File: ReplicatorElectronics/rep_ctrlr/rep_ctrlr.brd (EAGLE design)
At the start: 100 x 80 mm, 108 parts, among them IC1 MICROCHIP_PIC32MX7X5F256L-PF, IC2 MICROCHIP_MCP6001-LT, IC3 MICROCHIP_MCP6001-LT, IC4 MICROCHIP_MCP6001-LT, IC5 MICROCHIP_MCP6001-LT, J1 ATX24RH, J10 SBH11-PBPC-D07-ST-BK, J11 SBH11-PBPC-D07-ST-BK, J12 SBH11-PBPC-D07-ST-BK, J13 SBH11-PBPC-D07-ST-BK, J14 SBH11-PBPC-D07-ST-BK, J15 SBH11-PBPC-D07-ST-BK, J16 SBH11-PBPC-D07-ST-BK, J17 SBH11-PBPC-D07-ST-BK, J18 SI-50170-F, J19 70553-0106, J3 FPS009-3003, J4 RJ11-2L-B, J6 SBH11-PBPC-D05-ST-BK, J7 SBH11-PBPC-D05-ST-BK, J8 SBH11-PBPC-D05-ST-BK, J9 SBH11-PBPC-D05-ST-BK, U18 LDS3985XX33, X1 CMR3XXT, X2 CMR3XXT

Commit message: 5/5/12: Routed good portion of the PHY. Work in progress.
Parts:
- moved R42 155.6 mm to (78.9, 62.6)
- moved R35 154.5 mm to (82.0, 48.5), turned to 90 degrees
- moved R45 153.2 mm to (64.8, 58.5)
- moved R41 150.0 mm to (79.0, 64.9), turned to 180 degrees
- moved R34 147.2 mm to (79.0, 48.5), turned to 90 degrees
- moved R33 140.3 mm to (76.0, 48.0), turned to 90 degrees
- moved C27 137.5 mm to (73.8, 61.2), turned to 90 degrees
- moved R31 133.4 mm to (80.5, 52.0), turned to 90 degrees
- moved R32 133.2 mm to (73.0, 48.2), turned to 90 degrees
- moved C29 131.9 mm to (67.6, 53.5)
- moved C28 130.6 mm to (76.0, 61.2), turned to 90 degrees
- moved C25 129.0 mm to (68.5, 47.5), turned to 180 degrees
- moved C26 128.8 mm to (69.8, 60.0), turned to 180 degrees
- moved R30 126.4 mm to (77.5, 52.0), turned to 90 degrees
- moved C24 122.2 mm to (68.5, 50.2), turned to 180 degrees
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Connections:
- removed net N$22: C29.1
- new net ETXEN: IC1.67, R27.1
- net DGND: now also C29.1
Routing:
- net ECRSDV: track 0.00 -> 52.5 mm, vias 0 -> 4
- net NRST: track 0.00 -> 35.3 mm, vias 0 -> 2
- net N$38: track 0.00 -> 35.2 mm, vias 0 -> 2
- net ERXD0: track 0.00 -> 33.7 mm, vias 0 -> 2
- net EREFCLK: track 0.00 -> 29.5 mm, vias 0 -> 2
- net ETH_3_3V: track 0.00 -> 29.3 mm, vias 0 -> 2
- net N$39: track 0.00 -> 29.0 mm, vias 0 -> 2
- net ERXD1: track 0.00 -> 27.4 mm, vias 0 -> 2
- net LED1: track 0.00 -> 26.1 mm, vias 0 -> 1
- net ERXERR: track 0.00 -> 25.0 mm
- net N$30: track 0.00 -> 16.7 mm, vias 0 -> 2
- net N$33: track 0.00 -> 14.1 mm, vias 0 -> 2
- net N$32: track 0.00 -> 9.79 mm, vias 0 -> 2
- net EMDIO: track 0.00 -> 9.57 mm, vias 0 -> 2
- net N$31: track 0.00 -> 9.49 mm, vias 0 -> 2
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- added copper zone on layer 1, net DGND
- added copper zone on layer 16, net DGND
- removed copper zone on layer 16, net GND

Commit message: 5/8/12: First complete PHY layout attempt. Other parts of board still require routing.
~ 2 hrs.
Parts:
- removed Q1: (no value), semicon-smd-ipc:SOT23
- removed R10, R11, R12, R9: 22, resistor:R0603
- removed U$1: PETERATMEGA644_LCD37, microtouch:PETERATMEGA644_LCD371MM
- moved R26 204.9 mm to (86.5, 44.8), turned to 90 degrees
- moved R25 202.6 mm to (88.0, 41.2), turned to 90 degrees
- moved R38 177.4 mm to (71.2, 60.2), turned to 90 degrees
- moved R39 175.7 mm to (64.5, 60.2), turned to 90 degrees
- moved R37 170.2 mm to (69.0, 60.2), turned to 90 degrees
- moved R44 170.2 mm to (84.4, 49.4), turned to 180 degrees
- moved C23 167.0 mm to (82.5, 67.8), turned to 90 degrees
- moved C22 157.3 mm to (77.2, 67.9), turned to 90 degrees
- moved R43 133.5 mm to (55.7, 60.8), turned to 180 degrees
- moved R36 46.0 mm to (63.8, 54.5), turned to 90 degrees
- moved R27 39.2 mm to (85.0, 41.2), turned to 90 degrees
- moved R40 24.5 mm to (66.8, 60.2)
- moved C28 19.4 mm to (59.5, 51.0), turned to 0 degrees
- moved C24 16.5 mm to (53.2, 56.5)
- moved C25 16.4 mm to (53.0, 52.8)
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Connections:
- removed net LCD_LED: Q1.1
- removed net N$1: R9.2, U$1.17
- removed net N$10: Q1.3, R10.1, R11.1, R12.1, R9.1
- removed net N$3: R10.2, U$1.18
- removed net N$4: R11.2, U$1.19
- removed net N$6: R12.2, U$1.20
- new net N$54: IC1.79
- new net N$55: IC1.80
- net A0: no longer U$1.8
- net DB0: no longer U$1.1
- net DB1: no longer U$1.2
- net DB10: no longer U$1.23
- net DB11: no longer U$1.24
- net DB14: no longer IC1.79, U$1.25
- net DB15: no longer IC1.80, U$1.26
- net DB16: no longer U$1.27, U$1.29
- net DB17: no longer U$1.28, U$1.30
- net DB2: no longer U$1.3
- net DB3: no longer U$1.4
- net DB4: no longer U$1.22
- net DB5: no longer U$1.35
- net DB6: no longer U$1.36
- net DB7: no longer U$1.37
- net DGND: now also J10.10, J10.12, J11.10, J11.12, J12.10, J12.12, J13.10, J13.12, J14.10, J14.12, J15.10, J15.12, J16.10, J16.12, J17.10, J17.12; no longer Q1.2, U$1.11, U$1.21, U$1.34, U$1.5
- net ENC_3_3V: now also J10.14, J11.14, J12.14, J13.14, J14.14, J15.14, J16.14, J17.14
- net GND: now also J10.2, J10.4, J10.6, J11.2, J11.4, J11.6, J12.2, J12.4, J12.6, J13.2, J13.4, J13.6, J14.2, J14.4, J14.6, J15.2, J15.4, J15.6, J16.2, J16.4, J16.6, J17.2, J17.4, J17.6
- net LCD_CS: no longer U$1.7
- net LCD_RD: no longer U$1.10
- net LCD_RST: no longer U$1.31
- net LCD_WR: no longer U$1.9
- net SERVO0: now also J10.8
- net SERVO1: now also J11.8
- net SERVO2: now also J12.8
- net SERVO3: now also J13.8
- net SERVO4: now also J14.8
- net SERVO5: now also J15.8
- net SERVO6: now also J16.8
- net SERVO7: now also J17.8
- net VCC: no longer U$1.16, U$1.32, U$1.33, U$1.6
- net X+: no longer U$1.12
- net X-: no longer U$1.14
- net Y+: no longer U$1.13
- net Y-: no longer U$1.15
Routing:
- net ENC_3_3V: track 9.47 -> 112.5 mm, vias 1 -> 5
- net ENC_SCK: track 0.00 -> 57.5 mm
- net ENC_MOSI: track 0.00 -> 57.1 mm
- net ENC_MISO: track 0.00 -> 56.4 mm
- net N$36: track 0.00 -> 51.0 mm, vias 0 -> 4
- net LED2: track 7.83 -> 57.0 mm, vias 0 -> 3
- net N$37: track 0.00 -> 40.7 mm, vias 0 -> 2
- net ETXD0: track 0.00 -> 39.8 mm, vias 0 -> 2
- net N$34: track 0.00 -> 36.9 mm, vias 0 -> 2
- net ETXD1: track 0.00 -> 35.9 mm, vias 0 -> 2
- net N$35: track 0.00 -> 32.6 mm, vias 0 -> 1
- net ETH_3_3V: track 29.3 -> 53.0 mm, vias 2 -> 5
- net N$23: track 0.00 -> 23.0 mm, vias 0 -> 2
- net ETXEN: track 0.00 -> 19.4 mm, vias 0 -> 2
- net N$25: track 0.00 -> 17.4 mm, vias 0 -> 2
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- added copper zone on layer 16, net 5V_SERVO
- added copper zone on layer 1, net ENC_3_3V
- added copper zone on layer 1, net ETH_3_3V

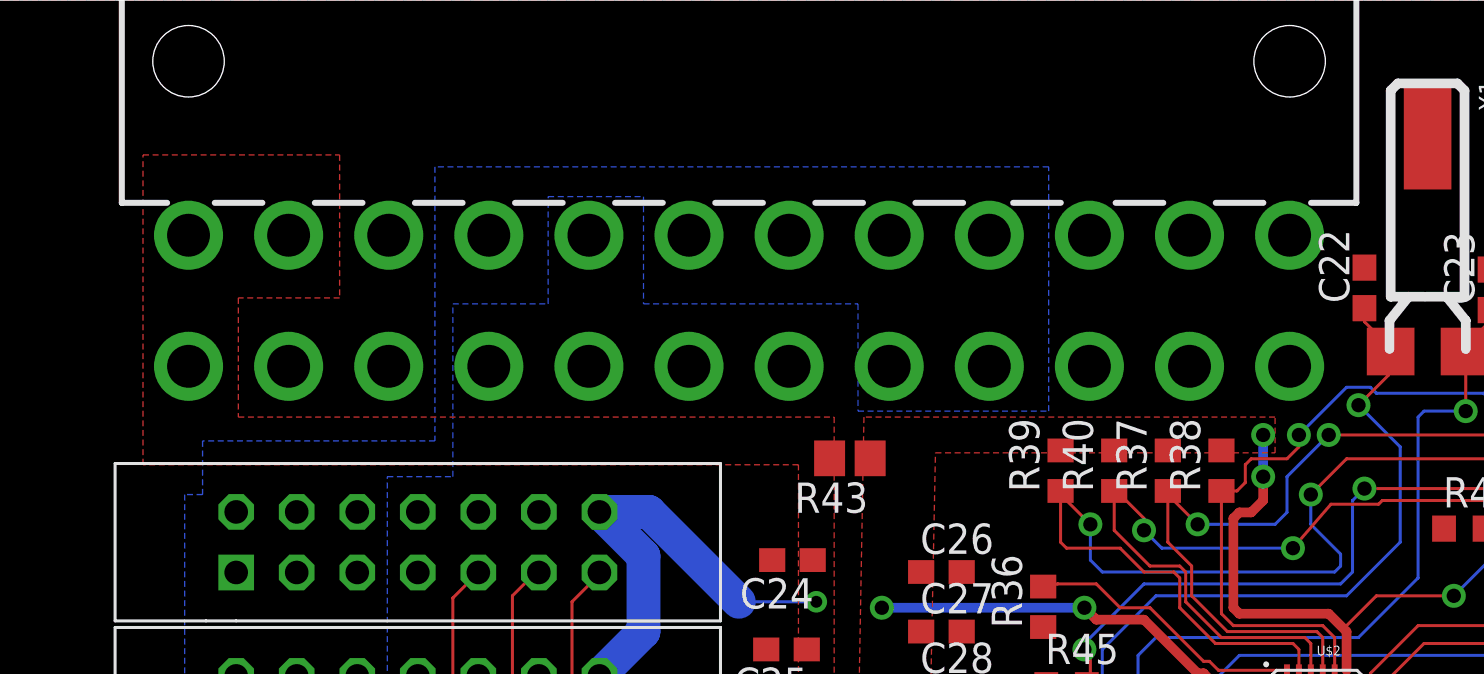
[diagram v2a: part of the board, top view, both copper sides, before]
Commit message: 5/8/12: Tied last 3.3V pin on ATX conn to ENC_3_3V
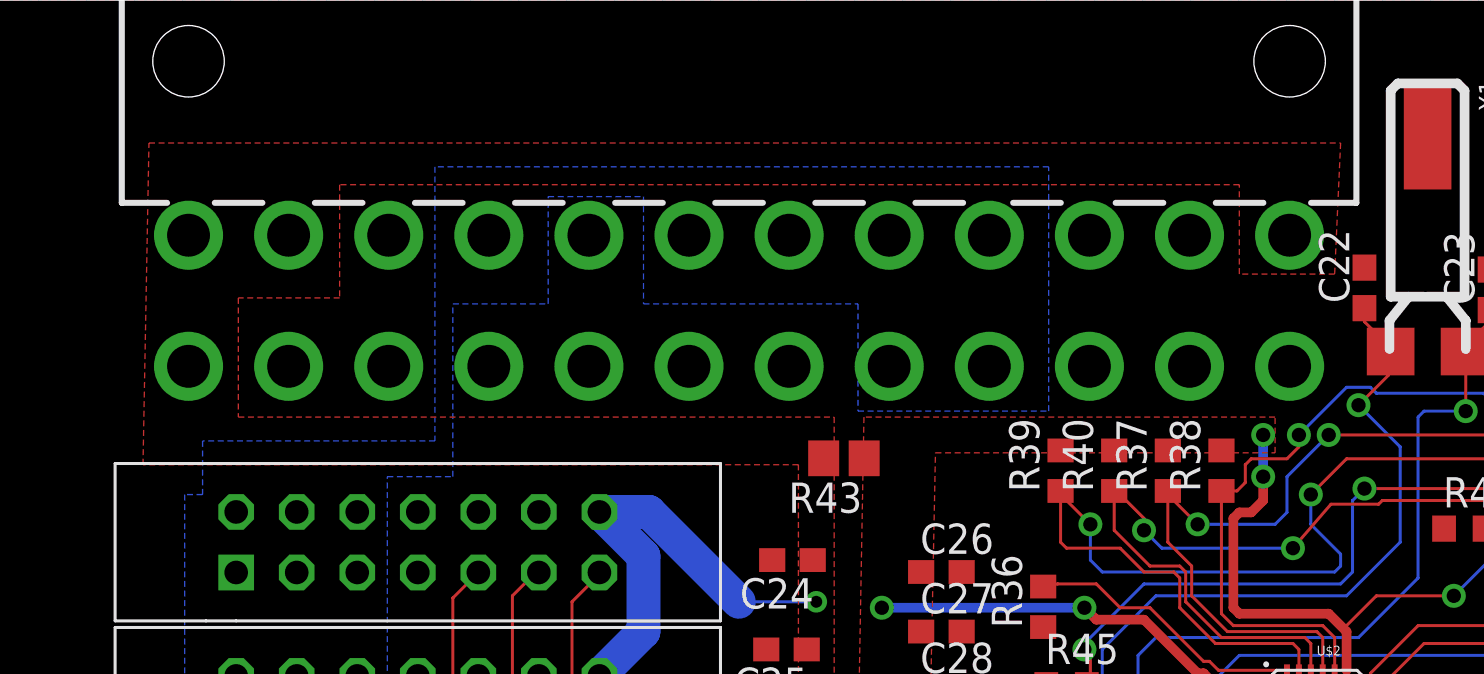
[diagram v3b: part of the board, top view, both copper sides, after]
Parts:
- moved R43 0.25 mm to (55.4, 60.8)
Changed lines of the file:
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@@
 </element>
 <element name="J19" library="70553-0109" package="70553-0109" value="70553-0106" x="57.76" y="-0.05" rot="R90"/>
-<element name="R43" library="resistor" package="R0805" value="FERRITE" x="55.66" y="60.77" rot="R180"/>
+<element name="R43" library="resistor" package="R0805" value="FERRITE" x="55.41" y="60.77" rot="R180"/>
 <element name="C31" library="rcl" package="R/2012-12R" value="4.7uF" x="55.75" y="46"/>
 <element name="C32" library="rcl" package="R/2012-12R" value="4.7uF" x="55.75" y="38.5"/>
@@
 <contactref element="J11" pad="14"/>
 <polygon width="0.127" layer="1" isolate="0.254">
-<vertex x="34.25" y="73.5"/>
+<vertex x="76.25" y="74"/>
+<vertex x="76" y="68.5"/>
+<vertex x="72" y="68.5"/>
+<vertex x="72" y="72.25"/>
+<vertex x="34.25" y="72.25"/>
 <vertex x="34.25" y="67.5"/>
 <vertex x="30" y="67.5"/>
@@
 <vertex x="53.5" y="60.5"/>
 <vertex x="26" y="60.5"/>
-<vertex x="26" y="73.5"/>
+<vertex x="26.25" y="74"/>
 </polygon>
 <wire x1="75" y1="48.125" x2="75" y2="46.75" width="0.4064" layer="1"/>
@@
 <wire x1="47.5" y1="10.75" x2="47.5" y2="13.14" width="1.4224" layer="16"/>
 <wire x1="47.5" y1="13.14" x2="45.24" y2="15.4" width="1.4224" layer="16"/>
-<wire x1="54.81" y1="60.77" x2="74.11008125" y2="70.129740625" width="0" layer="19" extent="1-1"/>
 </signal>
 <signal name="SD_SP_MISO">

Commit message: 5/13/12: More PIC Routing
~5 hrs.
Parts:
- removed C22, C23: 20pf, rcl:C0603
- removed J3: FPS009-3003, con-yamaichi:FPS009-3003
- removed R3, R4, R5, R6, R7: 50k, resistor:R0603
- removed X1, X2: CMR3XXT, cmr3XXT:CMR309T
- added Q1, Q2: ASFL1, crystal:ASF
- added R10, R9: 10, resistor:R0603
- C18: value 20pf -> 0.1u; device rcl:C0603 -> resistor:C0603
- C19: value 20pf -> 0.1uF
- moved C19 185.7 mm to (84.0, 14.2)
- moved C18 176.9 mm to (89.5, 30.0)
- moved R8 92.2 mm to (18.7, 52.2), turned to 270 degrees
- moved J8 10.6 mm to (6.77, 45.4), turned to 180 degrees
- moved J7 10.5 mm to (14.2, 45.4), turned to 180 degrees
- moved J9 10.5 mm to (11.6, 34.6), turned to 0 degrees
- moved R32 0.25 mm to (73.0, 41.5)
- moved R46 0.25 mm to (52.2, 40.8)
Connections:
- removed net 5V: 5V.TP, C32.+, R46.1, U18.1
- removed net N$39: C23.1, U$2.P4, X1.P$1
- removed net N$7: J3.8, R4.1
- removed net N$8: J3.9, R3.1
- new net N$1: Q2.3, R9.2
- new net N$4: Q1.3, R10.2
- net 5V_USB: now also 5V.TP, C32.+, R46.1, U18.1
- net DGND: now also C18.2, C19.2, C31.-, C32.-, C33.2, J1.15, J1.17, J1.18, J1.19, J1.24, J1.3, J1.5, J1.7, J19.P$6, Q1.2, Q2.2, U18.2; no longer C22.2, C23.2, J3.3, J3.6, X1.P$4
- net GND: no longer C18.2, C19.2, C31.-, C32.-, C33.2, J1.15, J1.17, J1.18, J1.19, J1.24, J1.3, J1.5, J1.7, U18.2
- net N$38: now also R10.1; no longer C22.1, X1.P$3
- net PICCLKI: now also R9.1; no longer C18.1, X2.P$1
- net PICCLKO: no longer C19.1, X2.P$3
- net SD_CSN: no longer J3.1, R7.1
- net SD_SP_MISO: now also J19.P$3; no longer J3.7, R5.1
- net SD_SP_MOSI: now also J19.P$4; no longer J3.2, R6.1
- net SD_SP_SCK: now also J19.P$1; no longer J3.5
- net SP_CSN: now also J19.P$2
- net VCC: now also C18.1, C19.1, J19.P$5, Q1.4, Q2.4; no longer J3.4, R3.2, R4.2, R5.2, R6.2, R7.2
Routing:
- net 5V_SERVO: track 0.00 -> 245.5 mm, vias 0 -> 8
- net ENC1_CSN: track 0.00 -> 138.1 mm, vias 0 -> 1
- net SERVO2: track 0.00 -> 132.1 mm, vias 0 -> 3
- net ENC2_CSN: track 0.00 -> 131.0 mm, vias 0 -> 5
- net SERVO3: track 0.00 -> 128.0 mm, vias 0 -> 3
- net ENC3_CSN: track 0.00 -> 123.6 mm, vias 0 -> 5
- net 5V_USB: track 0.00 -> 118.8 mm, vias 0 -> 7
- net TEMP1_BUF: track 0.00 -> 77.8 mm, vias 0 -> 4
- net TEMP3_BUF: track 0.00 -> 77.3 mm, vias 0 -> 2
- net SERVO4: track 0.00 -> 67.0 mm, vias 0 -> 7
- net ENC7_CSN: track 0.00 -> 61.0 mm, vias 0 -> 3
- net SERVO5: track 0.00 -> 58.0 mm, vias 0 -> 5
- net SERVO6: track 0.00 -> 57.1 mm, vias 0 -> 5
- net SERVO1: track 0.00 -> 56.5 mm, vias 0 -> 1
- net ENC0_CSN: track 0.00 -> 56.0 mm, vias 0 -> 7
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- added copper zone on layer 1, net GND
- removed copper zone on layer 16, net 5V_SERVO
